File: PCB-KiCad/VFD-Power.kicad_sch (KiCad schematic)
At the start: 22 parts, among them IC1 74132D, IC2 XL6009, IC3 ZXBM5210, U3 R-78B5.0-2.0

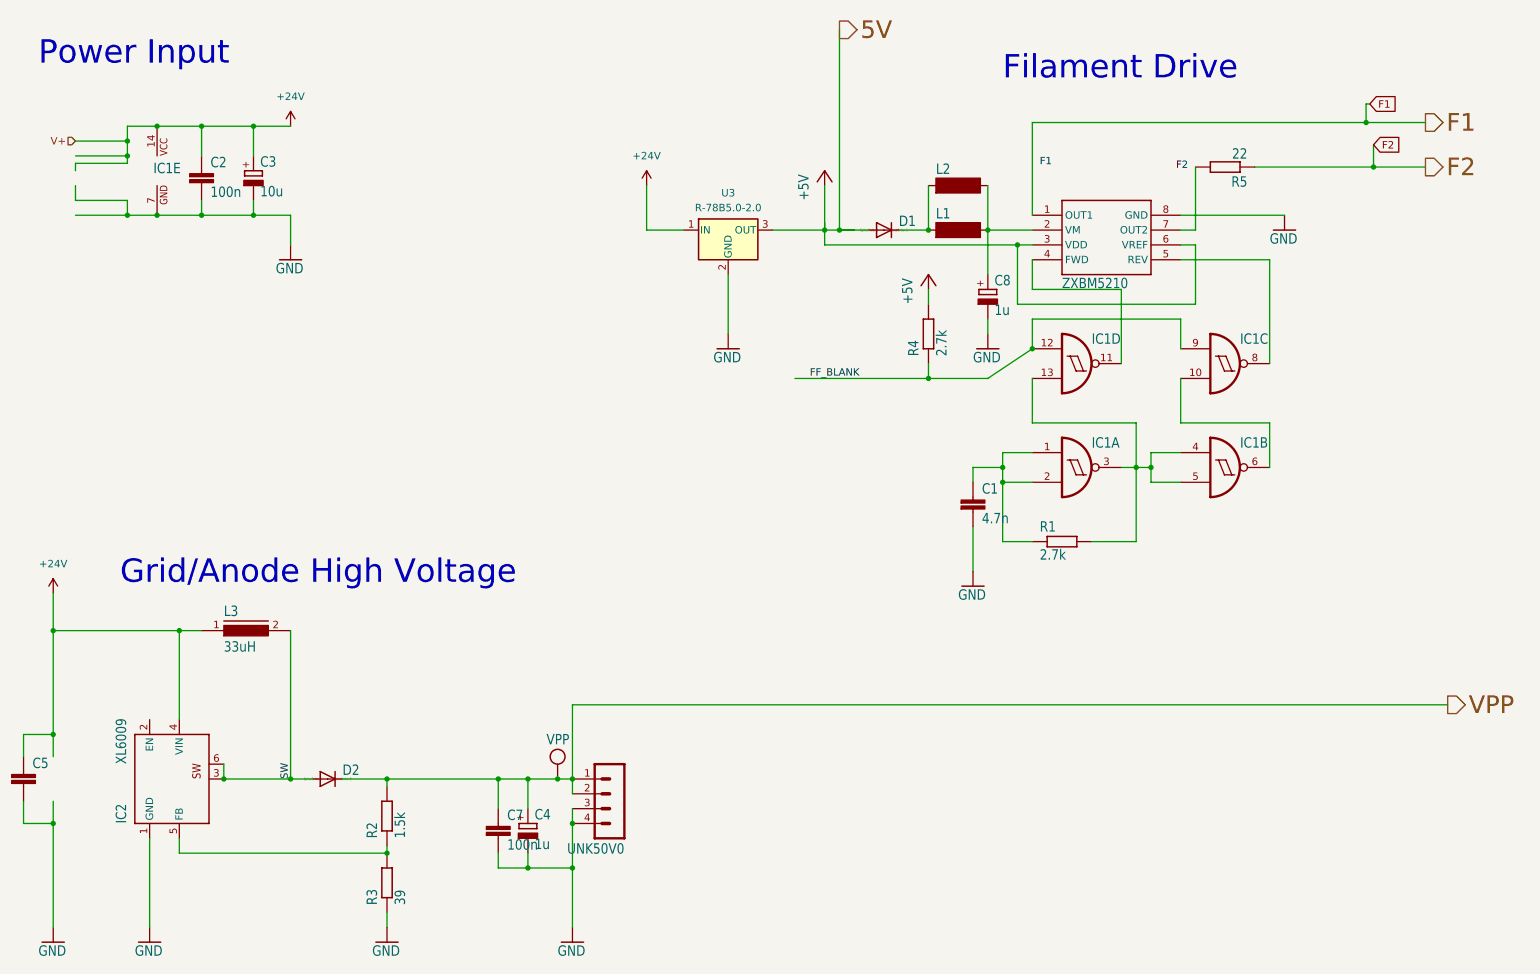
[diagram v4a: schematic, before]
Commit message: GP1294 evolves
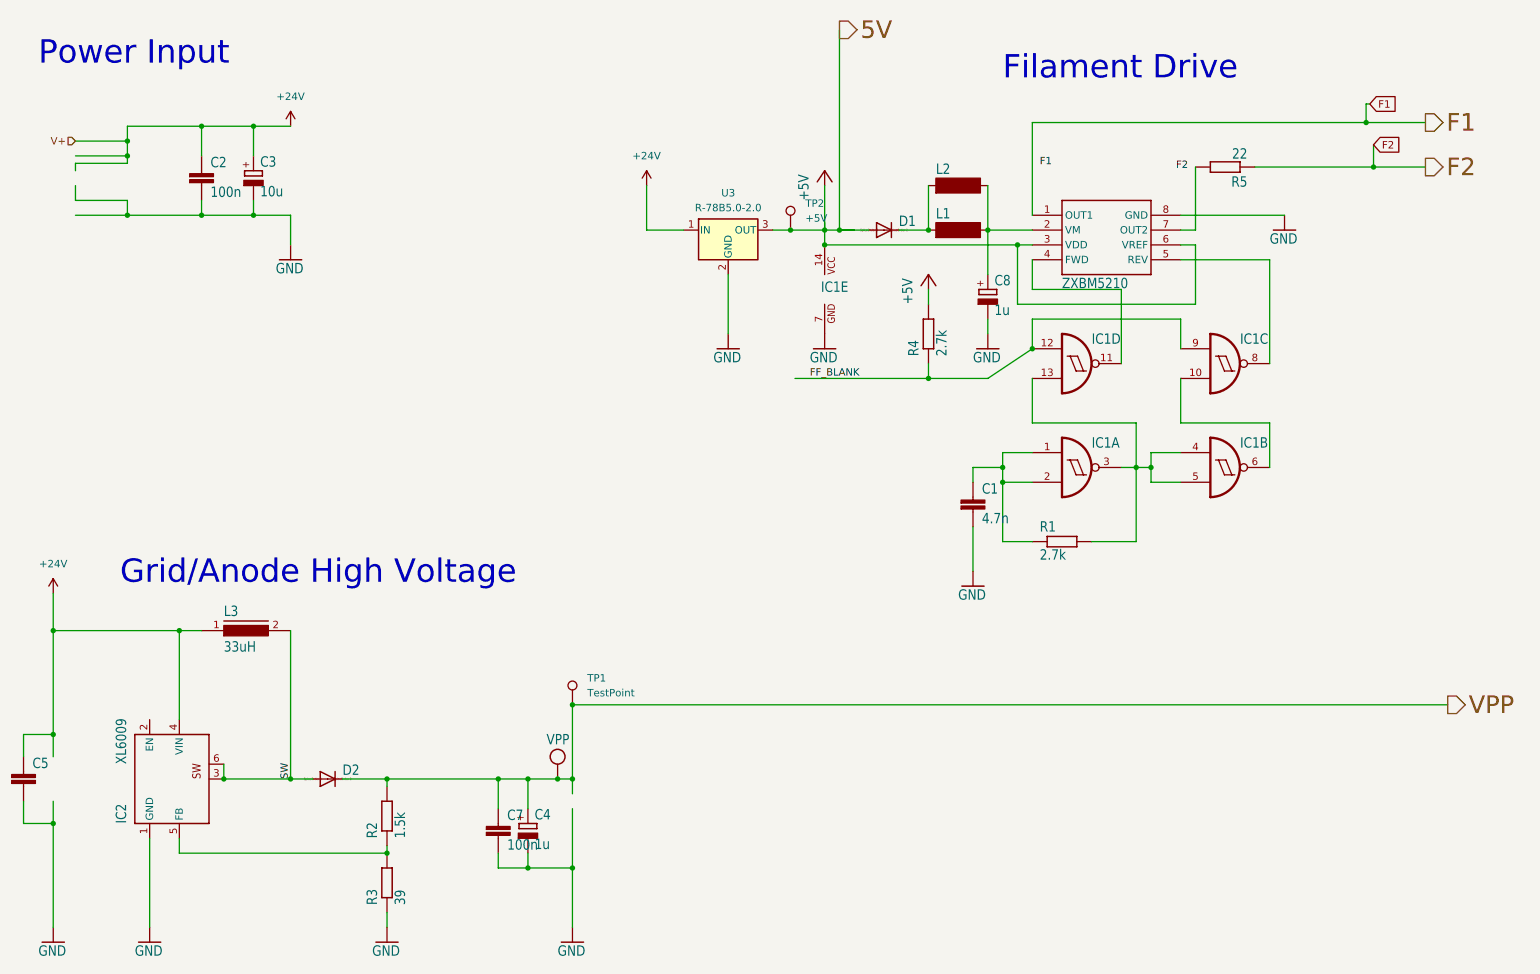
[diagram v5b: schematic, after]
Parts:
- removed UNK50V0: MA04-1, VFD-Power:MA04-1, symbol VFD-Power-eagle-import:MA04-1
- added TP1: TestPoint, TestPoint:TestPoint_Pad_2.0x2.0mm, symbol Connector:TestPoint
- added TP2: +5V, TestPoint:TestPoint_Pad_2.0x2.0mm, symbol Connector:TestPoint
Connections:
- net +24V: no longer IC1.14 (VCC)
- net +5V: now also IC1.14 (VCC), TP2.1
- net VPP: now also TP1.1
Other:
- moved on the sheet: IC1E
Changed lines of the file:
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@@
   (junction (at 196.85 73.66) (diameter 0) (color 0 0 0 0)
   )
-  (junction (at 118.11 154.94) (diameter 0) (color 0 0 0 0)
-  )
   (junction (at 63.5 35.56) (diameter 0) (color 0 0 0 0)
   )
@@
   (junction (at 118.11 162.56) (diameter 0) (color 0 0 0 0)
   )
+  (junction (at 155.448 53.34) (diameter 0) (color 0 0 0 0)
+  )
   (junction (at 54.61 35.56) (diameter 0) (color 0 0 0 0)
   )
-  (junction (at 46.99 35.56) (diameter 0) (color 0 0 0 0)
-  )
   (junction (at 217.17 93.98) (diameter 0) (color 0 0 0 0)
   )
@@
   (junction (at 29.21 154.94) (diameter 0) (color 0 0 0 0)
   )
+  (junction (at 118.11 134.62) (diameter 0) (color 0 0 0 0)
+  )
   (junction (at 179.07 78.74) (diameter 0) (color 0 0 0 0)
   )
   (junction (at 86.36 147.32) (diameter 0) (color 0 0 0 0)
   )
+  (junction (at 161.29 55.88) (diameter 0) (color 0 0 0 0)
+  )
   (junction (at 41.91 50.8) (diameter 0) (color 0 0 0 0)
   )
@@
   (junction (at 41.91 40.64) (diameter 0) (color 0 0 0 0)
   )
-  (junction (at 46.99 50.8) (diameter 0) (color 0 0 0 0)
-  )
-  (wire (pts (xy 46.99 50.8) (xy 54.61 50.8))
+  (wire (pts (xy 155.448 53.34) (xy 161.29 53.34))
+    (stroke (width 0) (type default))
+  )
+  (wire (pts (xy 41.91 50.8) (xy 54.61 50.8))
     (stroke (width 0.1524) (type solid))
   )
@@
     (stroke (width 0.1524) (type solid))
   )
-  (wire (pts (xy 118.11 154.94) (xy 118.11 162.56))
+  (wire (pts (xy 118.11 152.4) (xy 118.11 162.56))
     (stroke (width 0.1524) (type solid))
   )
@@
     (stroke (width 0.1524) (type solid))
   )
-  (wire (pts (xy 41.91 50.8) (xy 46.99 50.8))
-    (stroke (width 0.1524) (type solid))
-  )
   (wire (pts (xy 179.07 45.72) (xy 179.07 53.34))
     (stroke (width 0.1524) (type solid))
@@
     (stroke (width 0) (type default))
   )
-  (wire (pts (xy 118.11 152.4) (xy 118.11 154.94))
-    (stroke (width 0.1524) (type solid))
-  )
   (wire (pts (xy 179.07 78.74) (xy 156.21 78.74))
     (stroke (width 0.1524) (type solid))
@@
     (stroke (width 0.1524) (type solid))
   )
-  (wire (pts (xy 41.91 35.56) (xy 46.99 35.56))
+  (wire (pts (xy 41.91 35.56) (xy 54.61 35.56))
     (stroke (width 0.1524) (type solid))
   )
@@
     (stroke (width 0.1524) (type solid))
   )
-  (wire (pts (xy 46.99 35.56) (xy 54.61 35.56))
-    (stroke (width 0.1524) (type solid))
-  )
   (wire (pts (xy 196.85 106.68) (xy 191.77 106.68))
     (stroke (width 0.1524) (type solid))
@@
     (stroke (width 0.1524) (type solid))
   )
-  (wire (pts (xy 152.4 53.34) (xy 161.29 53.34))
+  (wire (pts (xy 152.4 53.34) (xy 155.448 53.34))
     (stroke (width 0) (type default))
   )
@@
     )
   )
+  (symbol (lib_id "Connector:TestPoint") (at 118.11 134.62 0) (unit 1)
+    (in_bom yes) (on_board yes) (dnp no) (fields_autoplaced)
+    (property "Reference" "TP1" (at 120.65 130.048 0)
+      (effects (font (size 1.27 1.27)) (justify left))
+    )
+    (property "Value" "TestPoint" (at 120.65 132.588 0)
+      (effects (font (size 1.27 1.27)) (justify left))
+    )
+    (property "Footprint" "TestPoint:TestPoint_Pad_2.0x2.0mm" (at 123.19 134.62 0)
+      (effects (font (size 1.27 1.27)) hide)
+    )
+    (property "Datasheet" "~" (at 123.19 134.62 0)
+      (effects (font (size 1.27 1.27)) hide)
+    )
+    (pin "1")
+    (instances
+      (project "GP1294-Teens4"
+        (path "/3de011e3-f89b-42a8-8637-1f4c3f0867fa/9e049bd2-8c7e-4a7a-b856-b0fbd11ae8df"
+          (reference "TP1") (unit 1)
+        )
+      )
+    )
+  )
   (symbol (lib_id "VFD-Power-eagle-import:R-EU_0411/15") (at 229.87 42.545 180) (unit 1)
     (in_bom yes) (on_board yes) (dnp no)
@@
         (path "/d66e9896-ee3f-419d-ab82-78a854ae4100"
           (reference "R4") (unit 1)
+        )
+      )
+    )
+  )
+  (symbol (lib_id "Connector:TestPoint") (at 155.448 53.34 0) (unit 1)
+    (in_bom yes) (on_board yes) (dnp no) (fields_autoplaced)
+    (property "Reference" "TP2" (at 157.988 48.768 0)
+      (effects (font (size 1.27 1.27)) (justify left))
+    )
+    (property "Value" "+5V" (at 157.988 51.308 0)
+      (effects (font (size 1.27 1.27)) (justify left))
+    )
+    (property "Footprint" "TestPoint:TestPoint_Pad_2.0x2.0mm" (at 160.528 53.34 0)
+      (effects (font (size 1.27 1.27)) hide)
+    )
+    (property "Datasheet" "~" (at 160.528 53.34 0)
+      (effects (font (size 1.27 1.27)) hide)
+    )
+    (pin "1")
+    (instances
+      (project "GP1294-Teens4"
+        (path "/3de011e3-f89b-42a8-8637-1f4c3f0867fa/9e049bd2-8c7e-4a7a-b856-b0fbd11ae8df"
+          (reference "TP2") (unit 1)
         )
       )
@@
     )
   )
+  (symbol (lib_id "VFD-Power-eagle-import:GND") (at 161.29 73.66 0) (unit 1)
+    (in_bom yes) (on_board yes) (dnp no)
+    (property "Reference" "#GND010" (at 161.29 73.66 0)
+      (effects (font (size 1.27 1.27)) hide)
+    )
+    (property "Value" "GND" (at 158.75 76.2 0)
+      (effects (font (size 1.778 1.5113)) (justify left bottom))
+    )
+    (property "Footprint" "" (at 161.29 73.66 0)
+      (effects (font (size 1.27 1.27)) hide)
+    )
+    (property "Datasheet" "" (at 161.29 73.66 0)
+      (effects (font (size 1.27 1.27)) hide)
+    )
+    (pin "1")
+    (instances
+      (project "GP1294-Teens4"
+        (path "/3de011e3-f89b-42a8-8637-1f4c3f0867fa/9e049bd2-8c7e-4a7a-b856-b0fbd11ae8df"
+          (reference "#GND010") (unit 1)
+        )
+      )
+    )
+  )
   (symbol (lib_id "VFD-Power-eagle-import:74132D") (at 229.87 76.2 0) (unit 3)
     (in_bom yes) (on_board yes) (dnp no)
@@
     )
   )
-  (symbol (lib_id "VFD-Power-eagle-import:MA04-1") (at 125.73 152.4 180) (unit 1)
-    (in_bom yes) (on_board yes) (dnp no)
-    (property "Reference" "UNK50V0" (at 127 158.242 0)
-      (effects (font (size 1.778 1.5113)) (justify left bottom))
-    )
-    (property "Value" "MA04-1" (at 127 142.24 0)
-      (effects (font (size 1.778 1.5113)) (justify left bottom) hide)
-    )
-    (property "Footprint" "VFD-Power:MA04-1" (at 125.73 152.4 0)
-      (effects (font (size 1.27 1.27)) hide)
-    )
-    (property "Datasheet" "" (at 125.73 152.4 0)
-      (effects (font (size 1.27 1.27)) hide)
-    )
-    (pin "1")
-    (pin "2")
-    (pin "3")
-    (pin "4")
-    (instances
-      (project "GP1294-Teens4"
-        (path "/3de011e3-f89b-42a8-8637-1f4c3f0867fa/9e049bd2-8c7e-4a7a-b856-b0fbd11ae8df"
-          (reference "UNK50V0") (unit 1)
-        )
-      )
-      (project "VFD-Power"
-        (path "/d66e9896-ee3f-419d-ab82-78a854ae4100"
-          (reference "UNK50V0") (unit 1)
-        )
-      )
-    )
-  )
   (symbol (lib_id "VFD-Power-eagle-import:GND") (at 240.03 53.34 0) (unit 1)
     (in_bom yes) (on_board yes) (dnp no)
@@
     )
   )
-  (symbol (lib_id "VFD-Power-eagle-import:74132D") (at 46.99 43.18 0) (unit 5)
-    (in_bom yes) (on_board yes) (dnp no)
-    (property "Reference" "IC1" (at 46.355 43.815 0)
-      (effects (font (size 1.778 1.5113)) (justify left bottom))
-    )
-    (property "Value" "74132D" (at 49.53 48.26 0)
+  (symbol (lib_id "VFD-Power-eagle-import:74132D") (at 161.29 63.5 0) (unit 5)
+    (in_bom yes) (on_board yes) (dnp no)
+    (property "Reference" "IC1" (at 160.655 64.135 0)
+      (effects (font (size 1.778 1.5113)) (justify left bottom))
+    )
+    (property "Value" "74132D" (at 163.83 68.58 0)
       (effects (font (size 1.778 1.5113)) (justify left bottom) hide)
     )
-    (property "Footprint" "VFD-Power:SO14" (at 46.99 43.18 0)
-      (effects (font (size 1.27 1.27)) hide)
-    )
-    (property "Datasheet" "" (at 46.99 43.18 0)
-      (effects (font (size 1.27 1.27)) hide)
-    )
+    (property "Footprint" "VFD-Power:SO14" (at 161.29 63.5 0)
+      (effects (font (size 1.27 1.27)) hide)
+    )
+    (property "Datasheet" "" (at 161.29 63.5 0)
+      (effects (font (size 1.27 1.27)) hide)
+    )

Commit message: Added SRC.
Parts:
- C4, C8: footprint VFD-Power:153CLV-0505 -> VFD-Power:C1206
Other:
- moved on the sheet: C4, C8
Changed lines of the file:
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@@
   (junction (at 214.63 93.98) (diameter 0) (color 0 0 0 0)
   )
+  (junction (at 112.522 162.56) (diameter 0) (color 0 0 0 0)
+  )
   (junction (at 54.61 50.8) (diameter 0) (color 0 0 0 0)
   )
@@
   (junction (at 86.36 160.02) (diameter 0) (color 0 0 0 0)
   )
-  (junction (at 110.49 162.56) (diameter 0) (color 0 0 0 0)
-  )
   (junction (at 161.29 53.34) (diameter 0) (color 0 0 0 0)
   )
@@
   (junction (at 105.41 147.32) (diameter 0) (color 0 0 0 0)
   )
+  (junction (at 112.522 147.32) (diameter 0) (color 0 0 0 0)
+  )
   (junction (at 118.11 162.56) (diameter 0) (color 0 0 0 0)
   )
@@
   (junction (at 189.23 53.34) (diameter 0) (color 0 0 0 0)
   )
-  (junction (at 110.49 147.32) (diameter 0) (color 0 0 0 0)
-  )
   (junction (at 29.21 121.92) (diameter 0) (color 0 0 0 0)
   )
@@
     (stroke (width 0) (type default))
   )
+  (wire (pts (xy 112.522 151.384) (xy 112.522 147.32))
+    (stroke (width 0) (type default))
+  )
   (wire (pts (xy 196.85 73.66) (xy 189.23 78.74))
     (stroke (width 0.1524) (type solid))
@@
     (stroke (width 0.1524) (type solid))
   )
-  (wire (pts (xy 189.23 60.96) (xy 189.23 53.34))
-    (stroke (width 0.1524) (type solid))
-  )
-  (wire (pts (xy 105.41 147.32) (xy 110.49 147.32))
+  (wire (pts (xy 189.23 59.69) (xy 189.23 53.34))
     (stroke (width 0.1524) (type solid))
   )
@@
     (stroke (width 0) (type default))
   )
+  (wire (pts (xy 112.522 162.56) (xy 118.11 162.56))
+    (stroke (width 0.1524) (type solid))
+  )
   (wire (pts (xy 163.83 19.05) (xy 163.83 53.34))
     (stroke (width 0) (type default))
@@
     (stroke (width 0.1524) (type solid))
   )
-  (wire (pts (xy 110.49 152.4) (xy 110.49 147.32))
-    (stroke (width 0.1524) (type solid))
-  )
   (wire (pts (xy 179.07 45.72) (xy 179.07 53.34))
     (stroke (width 0.1524) (type solid))
@@
     (stroke (width 0.1524) (type solid))
   )
-  (wire (pts (xy 189.23 71.12) (xy 189.23 68.58))
+  (wire (pts (xy 189.23 71.12) (xy 189.23 67.31))
     (stroke (width 0.1524) (type solid))
   )
@@
     (stroke (width 0.1524) (type solid))
   )
-  (wire (pts (xy 118.11 162.56) (xy 110.49 162.56))
-    (stroke (width 0.1524) (type solid))
-  )
-  (wire (pts (xy 105.41 162.56) (xy 110.49 162.56))
+  (wire (pts (xy 105.41 162.56) (xy 112.522 162.56))
     (stroke (width 0.1524) (type solid))
   )
@@
     (stroke (width 0.1524) (type solid))
   )
+  (wire (pts (xy 112.522 159.004) (xy 112.522 162.56))
+    (stroke (width 0) (type default))
+  )
   (wire (pts (xy 78.74 147.32) (xy 86.36 147.32))
     (stroke (width 0.1524) (type solid))
@@
     (stroke (width 0.1524) (type solid))
   )
+  (wire (pts (xy 112.522 147.32) (xy 115.57 147.32))
+    (stroke (width 0.1524) (type solid))
+  )
   (wire (pts (xy 222.25 73.66) (xy 222.25 68.58))
     (stroke (width 0.1524) (type solid))
@@
     (stroke (width 0.1524) (type solid))
   )
-  (wire (pts (xy 110.49 147.32) (xy 115.57 147.32))
+  (wire (pts (xy 105.41 147.32) (xy 112.522 147.32))
     (stroke (width 0.1524) (type solid))
   )
@@
   )
   (wire (pts (xy 24.13 143.51) (xy 24.13 139.7))
-    (stroke (width 0.1524) (type solid))
-  )
-  (wire (pts (xy 110.49 162.56) (xy 110.49 160.02))
     (stroke (width 0.1524) (type solid))
   )
@@
     )
   )
-  (symbol (lib_id "VFD-Power-eagle-import:CPOL-EU153CLV-0505") (at 110.49 154.94 0) (unit 1)
-    (in_bom yes) (on_board yes) (dnp no)
-    (property "Reference" "C4" (at 111.633 154.4574 0)
-      (effects (font (size 1.778 1.5113)) (justify left bottom))
-    )
-    (property "Value" "1u" (at 111.633 159.5374 0)
-      (effects (font (size 1.778 1.5113)) (justify left bottom))
-    )
-    (property "Footprint" "VFD-Power:153CLV-0505" (at 110.49 154.94 0)
-      (effects (font (size 1.27 1.27)) hide)
-    )
-    (property "Datasheet" "" (at 110.49 154.94 0)
+  (symbol (lib_id "VFD-Power-eagle-import:CPOL-EU153CLV-0505") (at 112.522 153.924 0) (unit 1)
+    (in_bom yes) (on_board yes) (dnp no)
+    (property "Reference" "C4" (at 113.665 153.4414 0)
+      (effects (font (size 1.778 1.5113)) (justify left bottom))
+    )
+    (property "Value" "1u" (at 113.665 158.5214 0)
+      (effects (font (size 1.778 1.5113)) (justify left bottom))
+    )
+    (property "Footprint" "VFD-Power:C1206" (at 112.522 153.924 0)
+      (effects (font (size 1.27 1.27)) hide)
+    )
+    (property "Datasheet" "" (at 112.522 153.924 0)
       (effects (font (size 1.27 1.27)) hide)
     )
@@
     )
   )
-  (symbol (lib_id "VFD-Power-eagle-import:CPOL-EU153CLV-0505") (at 189.23 63.5 0) (unit 1)
-    (in_bom yes) (on_board yes) (dnp no)
-    (property "Reference" "C8" (at 190.373 63.0174 0)
-      (effects (font (size 1.778 1.5113)) (justify left bottom))
-    )
-    (property "Value" "1u" (at 190.373 68.0974 0)
-      (effects (font (size 1.778 1.5113)) (justify left bottom))
-    )
-    (property "Footprint" "VFD-Power:153CLV-0505" (at 189.23 63.5 0)
-      (effects (font (size 1.27 1.27)) hide)
-    )
-    (property "Datasheet" "" (at 189.23 63.5 0)
-      (effects (font (size 1.27 1.27)) hide)
-    )
+  (symbol (lib_id "VFD-Power-eagle-import:CPOL-EU153CLV-0505") (at 189.23 62.23 0) (unit 1)
+    (in_bom yes) (on_board yes) (dnp no)
+    (property "Reference" "C8" (at 190.373 61.7474 0)
+      (effects (font (size 1.778 1.5113)) (justify left bottom))
+    )
+    (property "Value" "1u" (at 190.373 66.8274 0)
+      (effects (font (size 1.778 1.5113)) (justify left bottom))
+    )
+    (property "Footprint" "VFD-Power:C1206" (at 189.23 62.23 0)
+      (effects (font (size 1.27 1.27)) hide)
+    )
+    (property "Datasheet" "" (at 189.23 62.23 0)
+      (effects (font (size 1.27 1.27)) hide)
+    )
